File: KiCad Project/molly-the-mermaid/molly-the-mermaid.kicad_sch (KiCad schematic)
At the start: 8 parts, among them SW1 SW_Push, SW2 SW_Push, SW3 SW_Push, SW4 SW_Push, SW5 SW_Push, SW6 SW_Push, U1 SC0915

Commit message: First draft
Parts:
- added BT1: Battery, Connector_JST:JST_PH_S2B-PH-SM4-TB_1x02-1MP_P2.00mm_Horizontal, symbol Device:Battery
- added D2, D3, D4, D5, D6: WS2812B, LED_SMD:LED_WS2812B_PLCC4_5.0x5.0mm_P3.2mm, symbol LED:WS2812B
- added J1: SAO, Connector_PinSocket_2.54mm:PinSocket_2x03_P2.54mm_Vertical, symbol Connector_Generic:Conn_02x03_Counter_Clockwise
- D1: footprint (none) -> Diode_SMD:D_SOD-123F
- SW1, SW2, SW3, SW4, SW5, SW6: footprint (none) -> Button_Switch_SMD:SW_SPST_TL3342
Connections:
- net +BATT: now also BT1.1 (+)
- net GND: now also BT1.2 (-), D2.3 (VSS), D3.3 (VSS), D4.3 (VSS), D5.3 (VSS), D6.3 (VSS), J1.2 (Pin_2)
- net SAO1: now reaches U1.1 (UART0_TX/I2C0_SDA/SPI0_RX/GP0)
- net SAO1: now also J1.5 (Pin_5)
- net SAO2: now reaches U1.2 (UART0_RX/I2C0_SCL/GPI0_CSn/GP1)
- net SAO2: now also J1.6 (Pin_6)
- net LED_DATA_1: now reaches U1.29 (GP22)
- net LED_DATA_1: now also D2.4 (DIN)
- net +3V3: now reaches U1.37 (3V3_EN)
- net +3V3: now also D2.1 (VDD), D3.1 (VDD), D4.1 (VDD), D5.1 (VDD), D6.1 (VDD), J1.1 (Pin_1)
- net SDA: now reaches U1.6 (UART1_TX/I2C0_SDA/SPI0_RX/GP4)
- net SDA: now also J1.3 (Pin_3)
- net SCL: now reaches U1.7 (UART1_RX/I2C0_SCL/SPI0_CSn/GP5)
- net SCL: now also J1.4 (Pin_4)
- new net: D2.2 (DOUT), D3.4 (DIN)
- new net: D4.2 (DOUT), D5.4 (DIN)
- new net: D3.2 (DOUT), D4.4 (DIN)
- new net: D5.2 (DOUT), D6.4 (DIN)
- no-connect marks 0 -> 21
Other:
- note added: "Gamepad Controls"
- company: (none) -> GalaxyAllie
- title: (none) -> Molly the Mermaid

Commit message: 1.0 schematic
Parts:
- added C1, C2, C3, C4, C5: C, Capacitor_SMD:C_0805_2012Metric_Pad1.18x1.45mm_HandSolder, symbol Device:C
- added D10, D11, D12, D13, D14, D15, D16, D7, D8, D9: LED, LED_SMD:LED_0805_2012Metric_Pad1.15x1.40mm_HandSolder, symbol Device:LED
- added R1, R10, R2, R3, R4, R5, R6, R7, R8, R9: R, Resistor_SMD:R_0805_2012Metric_Pad1.20x1.40mm_HandSolder, symbol Device:R
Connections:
- net +3V3: now also C1.1, C2.1, C3.1, C4.1, C5.1
- net GND: now also C1.2, C2.2, C3.2, C4.2, C5.2, D10.1 (K), D11.1 (K), D12.1 (K), D13.1 (K), D14.1 (K), D15.1 (K), D16.1 (K), D7.1 (K), D8.1 (K), D9.1 (K)
- net at U1.19 (I2C1_SDA/SPI1_SCK/GP14): now also R1.2, R2.2, R3.2, R4.2, R5.2
- net at U1.20 (I2C1_SCL/SPI1_TX/GP15): now also R10.2, R6.2, R7.2, R8.2, R9.2
- new net: D14.2 (A), R8.1
- new net: D13.2 (A), R7.1
- new net: D7.2 (A), R1.1
- new net: D11.2 (A), R5.1
- new net: D9.2 (A), R3.1
- new net: D10.2 (A), R4.1
- new net: D15.2 (A), R9.1
- new net: D8.2 (A), R2.1
- new net: D12.2 (A), R6.1
- new net: D16.2 (A), R10.1
- no-connect marks 21 -> 19
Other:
- note added: "Add-on output (V1.69BIS)"
- note added: "Battery Pack (1.8-5.5V)"
- note added: "Left LEDs"
- note added: "Raspberry Pi Pico"
- note added: "Right LEDs"
- note added: "WS2812 LEDs and decoupling caps"
- moved on the sheet: D2, D3, D4, D5, D6, J1

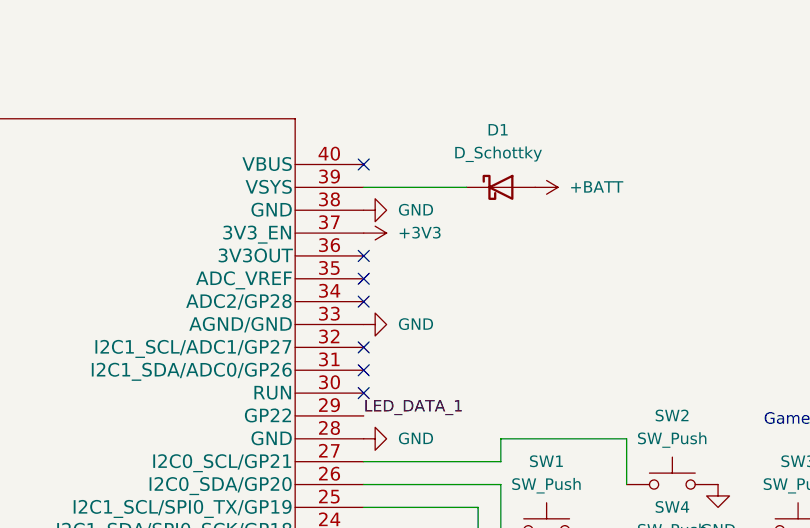
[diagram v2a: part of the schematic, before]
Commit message: fixed 3V3
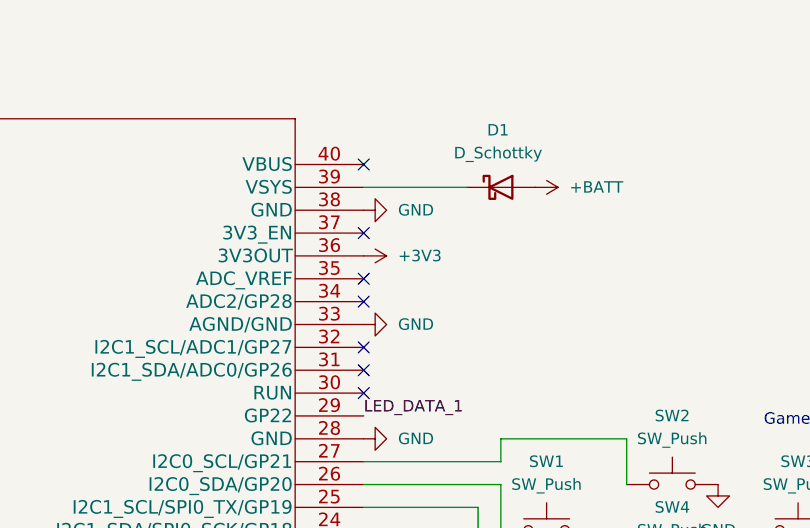
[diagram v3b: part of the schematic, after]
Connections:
- net +3V3: now also U1.36 (3V3OUT); no longer U1.37 (3V3_EN)
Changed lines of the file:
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@@
   (title_block
     (title "Molly the Mermaid")
-    (rev "1.0")
+    (rev "1.1")
     (company "GalaxyAllie")
   )
@@
   (no_connect (at 67.31 46.99))
   (no_connect (at 67.31 77.47))
+  (no_connect (at 171.45 44.45))
   (no_connect (at 67.31 69.85))
   (no_connect (at 171.45 57.15))
@@
   (no_connect (at 67.31 44.45))
   (no_connect (at 171.45 59.69))
-  (no_connect (at 171.45 46.99))
   (no_connect (at 171.45 62.23))
   (no_connect (at 171.45 36.83))
@@
     (pin "2")
   )
-  (symbol (lib_id "power:+3V3") (at 171.45 44.45 270) (unit 1)
-    (in_bom yes) (on_board yes) (fields_autoplaced)
-    (property "Reference" "#PWR0120" (id 0) (at 167.64 44.45 0)
-      (effects (font (size 1.27 1.27)) hide)
-    )
-    (property "Value" "+3V3" (id 1) (at 175.26 44.4499 90)
+  (symbol (lib_id "power:+3V3") (at 171.45 46.99 270) (unit 1)
+    (in_bom yes) (on_board yes) (fields_autoplaced)
+    (property "Reference" "#PWR0120" (id 0) (at 167.64 46.99 0)
+      (effects (font (size 1.27 1.27)) hide)
+    )
+    (property "Value" "+3V3" (id 1) (at 175.26 46.9899 90)
       (effects (font (size 1.27 1.27)) (justify left))
     )
-    (property "Footprint" "" (id 2) (at 171.45 44.45 0)
-      (effects (font (size 1.27 1.27)) hide)
-    )
-    (property "Datasheet" "" (id 3) (at 171.45 44.45 0)
-      (effects (font (size 1.27 1.27)) hide)
-    )
+    (property "Footprint" "" (id 2) (at 171.45 46.99 0)
+      (effects (font (size 1.27 1.27)) hide)
+    )
+    (property "Datasheet" "" (id 3) (at 171.45 46.99 0)
+      (effects (font (size 1.27 1.27)) hide)
+    )

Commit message: board draft
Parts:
- added R11: R, Resistor_SMD:R_0805_2012Metric_Pad1.20x1.40mm_HandSolder, symbol Device:R
- SW1: value SW_Push -> Left
- SW2: value SW_Push -> Up
- SW3: value SW_Push -> Right
- SW4: value SW_Push -> Down
- SW5: value SW_Push -> B
- SW6: value SW_Push -> A
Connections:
- net LED_DATA_1: now also R11.1; no longer D2.4 (DIN)
- new net: D2.4 (DIN), R11.2
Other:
- note added: "WS2812b LEDs and decoupling caps"
- note removed: "WS2812 LEDs and decoupling caps"
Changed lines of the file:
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@@
   (title_block
     (title "Molly the Mermaid")
-    (rev "1.1")
+    (rev "1.3")
     (company "GalaxyAllie")
   )
@@
     (effects (font (size 1.27 1.27)) (justify left bottom))
   )
-  (text "WS2812 LEDs and decoupling caps\n" (at 139.7 116.84 0)
+  (text "WS2812b LEDs and decoupling caps\n" (at 139.7 116.84 0)
     (effects (font (size 1.27 1.27)) (justify left bottom))
   )
@@
     (effects (font (size 1.27 1.27)) (justify right bottom))
   )
-  (label "LED_DATA_1" (at 97.79 148.59 180)
+  (label "LED_DATA_1" (at 90.17 148.59 180)
     (effects (font (size 1.27 1.27)) (justify right bottom))
   )
@@
     (in_bom yes) (on_board yes)
     (property "Reference" "SW5" (id 0) (at 234.95 76.2 0))
-    (property "Value" "SW_Push" (id 1) (at 234.95 78.74 0))
+    (property "Value" "B" (id 1) (at 234.95 78.74 0))
     (property "Footprint" "Button_Switch_SMD:SW_SPST_TL3342" (id 2) (at 234.95 78.74 0)
       (effects (font (size 1.27 1.27)) hide)
@@
     (in_bom yes) (on_board yes) (fields_autoplaced)
     (property "Reference" "SW4" (id 0) (at 205.74 74.93 0))
-    (property "Value" "SW_Push" (id 1) (at 205.74 77.47 0))
+    (property "Value" "Down" (id 1) (at 205.74 77.47 0))
     (property "Footprint" "Button_Switch_SMD:SW_SPST_TL3342" (id 2) (at 205.74 77.47 0)
       (effects (font (size 1.27 1.27)) hide)
@@
     (in_bom yes) (on_board yes) (fields_autoplaced)
     (property "Reference" "SW1" (id 0) (at 191.77 69.85 0))
-    (property "Value" "SW_Push" (id 1) (at 191.77 72.39 0))
+    (property "Value" "Left" (id 1) (at 191.77 72.39 0))
     (property "Footprint" "Button_Switch_SMD:SW_SPST_TL3342" (id 2) (at 191.77 72.39 0)
       (effects (font (size 1.27 1.27)) hide)
@@
     (in_bom yes) (on_board yes) (fields_autoplaced)
     (property "Reference" "SW3" (id 0) (at 219.71 69.85 0))
-    (property "Value" "SW_Push" (id 1) (at 219.71 72.39 0))
+    (property "Value" "Right" (id 1) (at 219.71 72.39 0))
     (property "Footprint" "Button_Switch_SMD:SW_SPST_TL3342" (id 2) (at 219.71 72.39 0)
       (effects (font (size 1.27 1.27)) hide)
@@
     (in_bom yes) (on_board yes) (fields_autoplaced)
     (property "Reference" "SW6" (id 0) (at 243.84 66.04 0))
-    (property "Value" "SW_Push" (id 1) (at 243.84 68.58 0))
+    (property "Value" "A" (id 1) (at 243.84 68.58 0))
     (property "Footprint" "Button_Switch_SMD:SW_SPST_TL3342" (id 2) (at 243.84 68.58 0)
       (effects (font (size 1.27 1.27)) hide)
@@
     )
     (pin "1")
+  )
+  (symbol (lib_id "Device:R") (at 93.98 148.59 90) (unit 1)
+    (in_bom yes) (on_board yes) (fields_autoplaced)
+    (property "Reference" "R11" (id 0) (at 93.98 142.24 90))
+    (property "Value" "R" (id 1) (at 93.98 144.78 90))
+    (property "Footprint" "Resistor_SMD:R_0805_2012Metric_Pad1.20x1.40mm_HandSolder" (id 2) (at 93.98 150.368 90)
+      (effects (font (size 1.27 1.27)) hide)
+    )
+    (property "Datasheet" "~" (id 3) (at 93.98 148.59 0)
+      (effects (font (size 1.27 1.27)) hide)
+    )
+    (pin "1")
+    (pin "2")
   )
   (symbol (lib_id "power:GND") (at 121.92 133.35 0) (unit 1)
@@
     (in_bom yes) (on_board yes) (fields_autoplaced)
     (property "Reference" "SW2" (id 0) (at 205.74 64.77 0))
-    (property "Value" "SW_Push" (id 1) (at 205.74 67.31 0))
+    (property "Value" "Up" (id 1) (at 205.74 67.31 0))
     (property "Footprint" "Button_Switch_SMD:SW_SPST_TL3342" (id 2) (at 205.74 67.31 0)
       (effects (font (size 1.27 1.27)) hide)
@@
       (reference "R10") (unit 1) (value "R") (footprint "Resistor_SMD:R_0805_2012Metric_Pad1.20x1.40mm_HandSolder")
     )
+    (path "/abfbeee5-7ba5-451d-b146-bd6f6dc9da81"
+      (reference "R11") (unit 1) (value "R") (footprint "Resistor_SMD:R_0805_2012Metric_Pad1.20x1.40mm_HandSolder")
+    )
     (path "/22c60e6b-0f47-483a-8cb3-55b3b36eddeb"
-      (reference "SW1") (unit 1) (value "SW_Push") (footprint "Button_Switch_SMD:SW_SPST_TL3342")
+      (reference "SW1") (unit 1) (value "Left") (footprint "Button_Switch_SMD:SW_SPST_TL3342")
     )
     (path "/fbe3a5a7-0c14-4855-a628-e3caecbd02ae"
-      (reference "SW2") (unit 1) (value "SW_Push") (footprint "Button_Switch_SMD:SW_SPST_TL3342")
+      (reference "SW2") (unit 1) (value "Up") (footprint "Button_Switch_SMD:SW_SPST_TL3342")
     )
     (path "/43f13bcc-0e76-43e3-9806-42cc2a9a7afa"
-      (reference "SW3") (unit 1) (value "SW_Push") (footprint "Button_Switch_SMD:SW_SPST_TL3342")
+      (reference "SW3") (unit 1) (value "Right") (footprint "Button_Switch_SMD:SW_SPST_TL3342")
     )
     (path "/1050c6c0-ea3c-47ab-a93f-3dd0584710f0"
-      (reference "SW4") (unit 1) (value "SW_Push") (footprint "Button_Switch_SMD:SW_SPST_TL3342")
+      (reference "SW4") (unit 1) (value "Down") (footprint "Button_Switch_SMD:SW_SPST_TL3342")
     )
     (path "/066e6826-06f3-4301-9ead-cbf238ae91aa"
-      (reference "SW5") (unit 1) (value "SW_Push") (footprint "Button_Switch_SMD:SW_SPST_TL3342")
+      (reference "SW5") (unit 1) (value "B") (footprint "Button_Switch_SMD:SW_SPST_TL3342")
     )
     (path "/9f6d7470-2459-4805-b70c-79a6d6a69535"
-      (reference "SW6") (unit 1) (value "SW_Push") (footprint "Button_Switch_SMD:SW_SPST_TL3342")
+      (reference "SW6") (unit 1) (value "A") (footprint "Button_Switch_SMD:SW_SPST_TL3342")
     )
     (path "/d4eb17c8-d7d9-4c8c-aada-ab472254d958"

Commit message: add mounting holes
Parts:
- added H1, H2: MountingHole, MountingHole:MountingHole_2.2mm_M2, symbol Mechanical:MountingHole
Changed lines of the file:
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@@
     (pin "2")
+  )
+  (symbol (lib_id "Mechanical:MountingHole") (at 247.65 38.1 0) (unit 1)
+    (in_bom yes) (on_board yes) (fields_autoplaced)
+    (property "Reference" "H2" (id 0) (at 250.19 36.8299 0)
+      (effects (font (size 1.27 1.27)) (justify left))
+    )
+    (property "Value" "MountingHole" (id 1) (at 250.19 39.3699 0)
+      (effects (font (size 1.27 1.27)) (justify left))
+    )
+    (property "Footprint" "MountingHole:MountingHole_2.2mm_M2" (id 2) (at 247.65 38.1 0)
+      (effects (font (size 1.27 1.27)) hide)
+    )
+    (property "Datasheet" "~" (id 3) (at 247.65 38.1 0)
+      (effects (font (size 1.27 1.27)) hide)
+    )
   )
   (symbol (lib_id "power:GND") (at 67.31 80.01 270) (unit 1)
@@
     )
     (pin "1")
+  )
+  (symbol (lib_id "Mechanical:MountingHole") (at 247.65 27.94 0) (unit 1)
+    (in_bom yes) (on_board yes) (fields_autoplaced)
+    (property "Reference" "H1" (id 0) (at 250.19 26.6699 0)
+      (effects (font (size 1.27 1.27)) (justify left))
+    )
+    (property "Value" "MountingHole" (id 1) (at 250.19 29.2099 0)
+      (effects (font (size 1.27 1.27)) (justify left))
+    )
+    (property "Footprint" "MountingHole:MountingHole_2.2mm_M2" (id 2) (at 247.65 27.94 0)
+      (effects (font (size 1.27 1.27)) hide)
+    )
+    (property "Datasheet" "~" (id 3) (at 247.65 27.94 0)
+      (effects (font (size 1.27 1.27)) hide)
+    )
   )
   (symbol (lib_id "Device:C") (at 177.8 129.54 0) (unit 1)
@@
       (reference "D16") (unit 1) (value "LED") (footprint "LED_SMD:LED_0805_2012Metric_Pad1.15x1.40mm_HandSolder")
     )
+    (path "/58828a74-0368-455b-bb0f-ed809146dee8"
+      (reference "H1") (unit 1) (value "MountingHole") (footprint "MountingHole:MountingHole_2.2mm_M2")
+    )
+    (path "/3b791526-4025-4ae9-8e00-b500303eec8c"
+      (reference "H2") (unit 1) (value "MountingHole") (footprint "MountingHole:MountingHole_2.2mm_M2")
+    )
     (path "/3850c140-ad46-4010-826a-b219f2a1f452"

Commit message: Added component values to schematic
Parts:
- C1, C2, C3, C4, C5: value C -> C 0.1uF
- R1, R10, R11, R2, R3, R4, R5, R6, R7, R8, R9: value R -> R470
